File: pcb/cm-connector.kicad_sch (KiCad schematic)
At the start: 16 parts, among them J1 SODIMM-200, J2 Debug Connector/DNP

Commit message: remove components from the BOM which are DNP
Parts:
- J1, TP1, TP10, TP11, TP12, TP13, TP2, TP3, TP4, TP5, TP6: now left out of the parts list

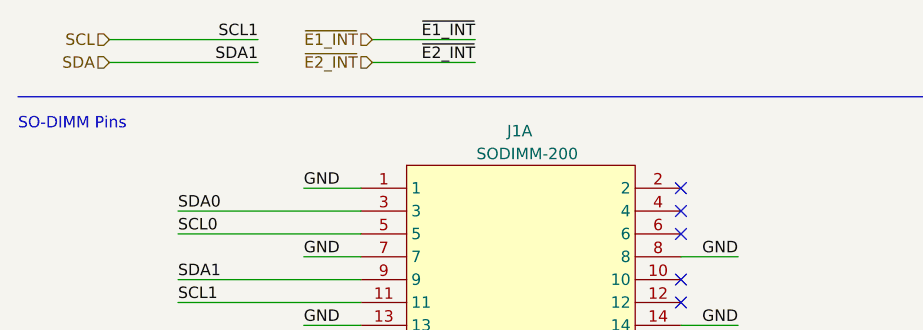
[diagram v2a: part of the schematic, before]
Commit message: Added jumper to swap I2C-0 with I2C-1 for the GPIO-Expanders
The GPIO expanders are using 0x20 and 0x21 as addresses and to avoid clashes with existing carrierboards I made the I2Cchannel switchable. Default is I2C-0 now
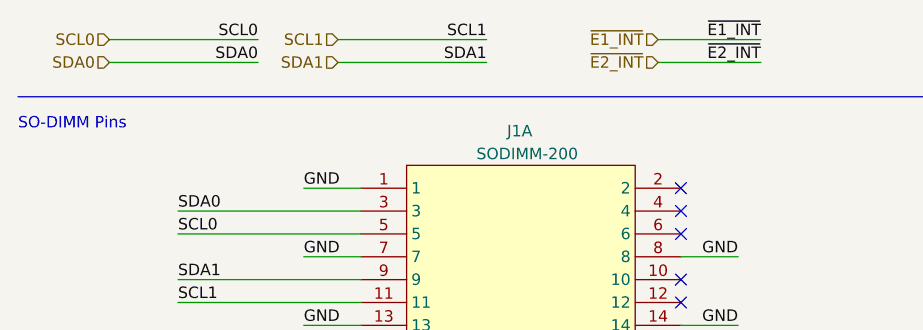
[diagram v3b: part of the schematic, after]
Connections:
- net SCL renamed SCL1
- net SDA renamed SDA1
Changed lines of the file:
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@@
     (stroke (width 0) (type default) (color 0 0 0 0))
   )
-  (wire (pts (xy 52.07 22.86) (xy 63.5 22.86))
+  (wire (pts (xy 83.82 22.86) (xy 95.25 22.86))
     (stroke (width 0) (type default) (color 0 0 0 0))
   )
@@
     (stroke (width 0) (type default) (color 0 0 0 0))
   )
+  (wire (pts (xy 48.26 20.32) (xy 64.77 20.32))
+    (stroke (width 0) (type default) (color 0 0 0 0))
+  )
   (wire (pts (xy 128.27 106.68) (xy 135.89 106.68))
     (stroke (width 0) (type default) (color 0 0 0 0))
@@
     (stroke (width 0) (type default) (color 0 0 0 0))
   )
-  (wire (pts (xy 52.07 20.32) (xy 63.5 20.32))
+  (wire (pts (xy 83.82 20.32) (xy 95.25 20.32))
     (stroke (width 0) (type default) (color 0 0 0 0))
   )
@@
     (stroke (width 0) (type default) (color 0 0 0 0))
   )
+  (wire (pts (xy 48.26 22.86) (xy 64.77 22.86))
+    (stroke (width 0) (type default) (color 0 0 0 0))
+  )
   (wire (pts (xy 66.04 160.02) (xy 86.36 160.02))
     (stroke (width 0) (type default) (color 0 0 0 0))
@@
     (effects (font (size 1.27 1.27)) (justify right bottom))
   )
-  (label "~{E2_INT}" (at 63.5 22.86 180)
+  (label "~{E2_INT}" (at 95.25 22.86 180)
     (effects (font (size 1.27 1.27)) (justify right bottom))
   )
@@
     (effects (font (size 1.27 1.27)) (justify right bottom))
   )
-  (label "~{E1_INT}" (at 63.5 20.32 180)
+  (label "~{E1_INT}" (at 95.25 20.32 180)
     (effects (font (size 1.27 1.27)) (justify right bottom))
   )
@@
     (effects (font (size 1.27 1.27)) (justify right bottom))
   )
+  (label "SCL1" (at 64.77 20.32 180)
+    (effects (font (size 1.27 1.27)) (justify right bottom))
+  )
   (label "V0SPI_MOSI" (at 30.48 77.47 0)
     (effects (font (size 1.27 1.27)) (justify left bottom))
@@
     (effects (font (size 1.27 1.27)) (justify left bottom))
   )
-  (label "SCL1" (at 39.37 20.32 180)
+  (label "SCL0" (at 39.37 20.32 180)
     (effects (font (size 1.27 1.27)) (justify right bottom))
   )
@@
     (effects (font (size 1.27 1.27)) (justify right bottom))
   )
+  (label "SDA1" (at 64.77 22.86 180)
+    (effects (font (size 1.27 1.27)) (justify right bottom))
+  )
   (label "GND" (at 129.54 71.12 0)
     (effects (font (size 1.27 1.27)) (justify left bottom))
   )
-  (label "SDA1" (at 39.37 22.86 180)
+  (label "SDA0" (at 39.37 22.86 180)
     (effects (font (size 1.27 1.27)) (justify right bottom))
   )
@@
     )
   )
-  (hierarchical_label "~{E2_INT}" (shape input) (at 52.07 22.86 180)
-    (effects (font (size 1.27 1.27)) (justify right))
-  )
-  (hierarchical_label "~{E1_INT}" (shape input) (at 52.07 20.32 180)
-    (effects (font (size 1.27 1.27)) (justify right))
-  )
-  (hierarchical_label "SDA" (shape input) (at 22.86 22.86 180)
-    (effects (font (size 1.27 1.27)) (justify right))
-  )
-  (hierarchical_label "SCL" (shape input) (at 22.86 20.32 180)
-    (effects (font (size 1.27 1.27)) (justify right))
-  )
+  (hierarchical_label "~{E2_INT}" (shape input) (at 83.82 22.86 180)
+    (effects (font (size 1.27 1.27)) (justify right))
+  )
+  (hierarchical_label "~{E1_INT}" (shape input) (at 83.82 20.32 180)
+    (effects (font (size 1.27 1.27)) (justify right))
+  )
+  (hierarchical_label "SDA1" (shape input) (at 48.26 22.86 180)
+    (effects (font (size 1.27 1.27)) (justify right))
+  )
+  (hierarchical_label "SDA0" (shape input) (at 22.86 22.86 180)
+    (effects (font (size 1.27 1.27)) (justify right))
+  )
+  (hierarchical_label "SCL0" (shape input) (at 22.86 20.32 180)
+    (effects (font (size 1.27 1.27)) (justify right))
+  )
+  (hierarchical_label "SCL1" (shape input) (at 48.26 20.32 180)
+    (effects (font (size 1.27 1.27)) (justify right))
+  )

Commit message: Refactored PCB Layer to have one dedicated GND Layer + rerouted traces + removed debug connector and added IO0 to the SO-DIMM connector + added decoupling caps and delay circuit for ESP32 module
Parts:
- removed J2: Debug Connector/DNP, Connector_PinSocket_2.54mm:PinSocket_1x06_P2.54mm_Vertical, symbol Connector:Conn_01x06_Male
- removed TP5: TP_3V3, TestPoint:TestPoint_Pad_D1.0mm, symbol Connector:TestPoint_Small
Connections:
- net IO0: now also J1.24
- no-connect marks 80 -> 79
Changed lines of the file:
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@@
   (junction (at 81.28 115.57) (diameter 0) (color 0 0 0 0)
   )
-  (junction (at 53.34 119.38) (diameter 0) (color 0 0 0 0)
-  )
   (junction (at 81.28 113.03) (diameter 0) (color 0 0 0 0)
   )
@@
   )
   (junction (at 109.22 113.03) (diameter 0) (color 0 0 0 0)
-  )
-  (junction (at 53.34 121.92) (diameter 0) (color 0 0 0 0)
   )
   (junction (at 109.22 110.49) (diameter 0) (color 0 0 0 0)
@@
   (no_connect (at 135.89 218.44))
   (no_connect (at 171.45 147.32))
-  (no_connect (at 86.36 64.77))
   (no_connect (at 135.89 149.86))
   (wire (pts (xy 66.04 199.39) (xy 86.36 199.39))
@@
     (stroke (width 0) (type default) (color 0 0 0 0))
   )
-  (wire (pts (xy 21.59 119.38) (xy 53.34 119.38))
+  (wire (pts (xy 27.94 109.22) (xy 53.34 109.22))
     (stroke (width 0) (type default) (color 0 0 0 0))
   )
@@
     (stroke (width 0) (type default) (color 0 0 0 0))
   )
-  (wire (pts (xy 21.59 121.92) (xy 53.34 121.92))
-    (stroke (width 0) (type default) (color 0 0 0 0))
-  )
   (wire (pts (xy 116.84 73.66) (xy 135.89 73.66))
     (stroke (width 0) (type default) (color 0 0 0 0))
@@
     (stroke (width 0) (type default) (color 0 0 0 0))
   )
+  (wire (pts (xy 27.94 116.84) (xy 53.34 116.84))
+    (stroke (width 0) (type default) (color 0 0 0 0))
+  )
   (wire (pts (xy 41.91 64.77) (xy 50.8 64.77))
     (stroke (width 0) (type default) (color 0 0 0 0))
@@
     (stroke (width 0) (type default) (color 0 0 0 0))
   )
-  (wire (pts (xy 21.59 116.84) (xy 53.34 116.84))
-    (stroke (width 0) (type default) (color 0 0 0 0))
-  )
   (wire (pts (xy 129.54 109.22) (xy 135.89 109.22))
     (stroke (width 0) (type default) (color 0 0 0 0))
@@
     (stroke (width 0) (type default) (color 0 0 0 0))
   )
+  (wire (pts (xy 86.36 64.77) (xy 92.71 64.77))
+    (stroke (width 0) (type default) (color 0 0 0 0))
+  )
   (wire (pts (xy 83.82 20.32) (xy 95.25 20.32))
     (stroke (width 0) (type default) (color 0 0 0 0))
@@
     (stroke (width 0) (type default) (color 0 0 0 0))
   )
-  (wire (pts (xy 21.59 109.22) (xy 53.34 109.22))
-    (stroke (width 0) (type default) (color 0 0 0 0))
-  )
   (wire (pts (xy 171.45 91.44) (xy 179.07 91.44))
     (stroke (width 0) (type default) (color 0 0 0 0))
@@
     (stroke (width 0) (type default) (color 0 0 0 0))
   )
-  (wire (pts (xy 66.04 104.14) (xy 66.04 121.92))
-    (stroke (width 0) (type default) (color 0 0 0 0))
-  )
   (wire (pts (xy 129.54 154.94) (xy 135.89 154.94))
     (stroke (width 0) (type default) (color 0 0 0 0))
   )
-  (wire (pts (xy 53.34 121.92) (xy 66.04 121.92))
-    (stroke (width 0) (type default) (color 0 0 0 0))
-  )
   (wire (pts (xy 177.8 132.08) (xy 171.45 132.08))
     (stroke (width 0) (type default) (color 0 0 0 0))
@@
     (stroke (width 0) (type default) (color 0 0 0 0))
   )
+  (wire (pts (xy 27.94 114.3) (xy 53.34 114.3))
+    (stroke (width 0) (type default) (color 0 0 0 0))
+  )
   (wire (pts (xy 53.34 119.38) (xy 54.61 119.38))
     (stroke (width 0) (type default) (color 0 0 0 0))
@@
     (stroke (width 0) (type default) (color 0 0 0 0))
   )
-  (wire (pts (xy 21.59 114.3) (xy 53.34 114.3))
-    (stroke (width 0) (type default) (color 0 0 0 0))
-  )
   (wire (pts (xy 189.23 241.3) (xy 189.23 243.84))
     (stroke (width 0) (type default) (color 0 0 0 0))
   )
+  (wire (pts (xy 27.94 111.76) (xy 53.34 111.76))
+    (stroke (width 0) (type default) (color 0 0 0 0))
+  )
   (wire (pts (xy 66.04 179.07) (xy 86.36 179.07))
     (stroke (width 0) (type default) (color 0 0 0 0))
@@
     (stroke (width 0) (type default) (color 0 0 0 0))
   )
-  (wire (pts (xy 21.59 111.76) (xy 53.34 111.76))
-    (stroke (width 0) (type default) (color 0 0 0 0))
-  )
   (wire (pts (xy 66.04 204.47) (xy 86.36 204.47))
     (stroke (width 0) (type default) (color 0 0 0 0))
@@
     (effects (font (size 1.27 1.27)) (justify left bottom))
   )
-  (label "TXD0" (at 40.64 116.84 180)
-    (effects (font (size 1.27 1.27)) (justify right bottom))
+  (label "TXD0" (at 27.94 116.84 0)
+    (effects (font (size 1.27 1.27)) (justify left bottom))
   )
   (label "GND" (at 177.8 223.52 180)
@@
     (effects (font (size 1.27 1.27)) (justify left bottom))
   )
-  (label "RXD0" (at 40.64 114.3 180)
-    (effects (font (size 1.27 1.27)) (justify right bottom))
+  (label "RXD0" (at 27.94 114.3 0)
+    (effects (font (size 1.27 1.27)) (justify left bottom))
   )
   (label "SCL1" (at 30.48 49.53 0)
@@
     (effects (font (size 1.27 1.27)) (justify right bottom))
   )
+  (label "IO0" (at 92.71 64.77 180)
+    (effects (font (size 1.27 1.27)) (justify right bottom))
+  )
   (label "SCL1" (at 64.77 20.32 180)
     (effects (font (size 1.27 1.27)) (justify right bottom))
@@
     (effects (font (size 1.27 1.27)) (justify right bottom))
   )
-  (label "IO0" (at 40.64 111.76 180)
-    (effects (font (size 1.27 1.27)) (justify right bottom))
+  (label "IO0" (at 27.94 111.76 0)
+    (effects (font (size 1.27 1.27)) (justify left bottom))
   )
   (label "GND" (at 44.45 67.31 0)
@@
     (effects (font (size 1.27 1.27)) (justify left bottom))
   )
-  (label "ESP_EN{slash}CM_RUN" (at 40.64 109.22 180)
-    (effects (font (size 1.27 1.27)) (justify right bottom))
+  (label "ESP_EN{slash}CM_RUN" (at 27.94 109.22 0)
+    (effects (font (size 1.27 1.27)) (justify left bottom))
   )
   (label "SCL1" (at 86.36 186.69 180)
@@
   (hierarchical_label "SCL1" (shape input) (at 48.26 20.32 180)
     (effects (font (size 1.27 1.27)) (justify right))
-  )
-  (symbol (lib_id "Connector:Conn_01x06_Male") (at 16.51 114.3 0) (unit 1)
-    (in_bom no) (on_board yes)
-    (property "Reference" "J2" (id 0) (at 26.67 101.6 0))
-    (property "Value" "Debug Connector/DNP" (id 1) (at 26.67 104.14 0))
-    (property "Footprint" "Connector_PinSocket_2.54mm:PinSocket_1x06_P2.54mm_Vertical" (id 2) (at 16.51 114.3 0)
-      (effects (font (size 1.27 1.27)) hide)
-    )
-    (property "Datasheet" "~" (id 3) (at 16.51 114.3 0)
-      (effects (font (size 1.27 1.27)) hide)
-    )
-    (pin "1")
-    (pin "2")
-    (pin "3")
-    (pin "4")
-    (pin "5")
-    (pin "6")
   )
   (symbol (lib_id "Connector:TestPoint_Small") (at 81.28 118.11 0) (unit 1)
@@
     )
     (property "Datasheet" "~" (id 3) (at 86.36 115.57 0)
-      (effects (font (size 1.27 1.27)) hide)
-    )
-    (pin "1")
-  )
-  (symbol (lib_id "Connector:TestPoint_Small") (at 53.34 121.92 0) (unit 1)
-    (in_bom no) (on_board yes)
-    (property "Reference" "TP5" (id 0) (at 49.53 120.65 0)
-      (effects (font (size 1.27 1.27)) (justify left))
-    )
-    (property "Value" "TP_3V3" (id 1) (at 55.88 123.19 0)
-      (effects (font (size 1.27 1.27)) (justify left))
-    )
-    (property "Footprint" "TestPoint:TestPoint_Pad_D1.0mm" (id 2) (at 58.42 121.92 0)
-      (effects (font (size 1.27 1.27)) hide)
-    )
-    (property "Datasheet" "~" (id 3) (at 58.42 121.92 0)
       (effects (font (size 1.27 1.27)) hide)
     )
@@
       (effects (font (size 1.27 1.27)) hide)
     )
-    (pin "1")
-  )
-  (symbol (lib_id "power:+3V3") (at 66.04 104.14 0) (unit 1)
-    (in_bom yes) (on_board yes) (fields_autoplaced)
-    (property "Reference" "#PWR0119" (id 0) (at 66.04 107.95 0)
-      (effects (font (size 1.27 1.27)) hide)
-    )
-    (property "Value" "+3V3" (id 1) (at 66.04 100.5355 0))
-    (property "Footprint" "" (id 2) (at 66.04 104.14 0)
-      (effects (font (size 1.27 1.27)) hide)
-    )
-    (property "Datasheet" "" (id 3) (at 66.04 104.14 0)
-      (effects (font (size 1.27 1.27)) hide)
-    )

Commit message: Convert to KiCad 7
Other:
- note added: "Test Point"
- note removed: "Debug Connector"
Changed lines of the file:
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@@
+    (stroke (width 0) (type default) (color 0 0 0 0))
+  )
+  (wire (pts (xy 53.34 119.38) (xy 53.34 121.92))
     (stroke (width 0) (type default) (color 0 0 0 0))
   )
@@
     (stroke (width 0) (type default) (color 0 0 0 0))
   )
-  (wire (pts (xy 54.61 119.38) (xy 54.61 127))
-    (stroke (width 0) (type default) (color 0 0 0 0))
-  )
   (wire (pts (xy 116.84 66.04) (xy 135.89 66.04))
     (stroke (width 0) (type default) (color 0 0 0 0))
@@
     (stroke (width 0) (type default) (color 0 0 0 0))
   )
-  (wire (pts (xy 53.34 119.38) (xy 54.61 119.38))
-    (stroke (width 0) (type default) (color 0 0 0 0))
-  )
   (wire (pts (xy 171.45 45.72) (xy 179.07 45.72))
     (stroke (width 0) (type default) (color 0 0 0 0))
@@
     (effects (font (size 1.27 1.27)) (justify left bottom))
   )
-  (text "Debug Connector" (at 13.97 95.25 0)
+  (text "Test Point" (at 13.97 95.25 0)
     (effects (font (size 1.27 1.27)) (justify left bottom))
   )
@@
       (effects (font (size 1.27 1.27)) (justify left))
     )
-    (property "Value" "TP_IO0" (id 1) (at 55.88 111.76 0)
+    (property "Value" "TP_IO0" (id 1) (at 54.61 111.76 0)
       (effects (font (size 1.27 1.27)) (justify left))
     )
@@
     (pin "1")
   )
-  (symbol (lib_id "power:GND") (at 54.61 127 0) (unit 1)
+  (symbol (lib_id "power:GND") (at 53.34 121.92 0) (unit 1)
     (in_bom yes) (on_board yes) (fields_autoplaced)
-    (property "Reference" "#PWR0118" (id 0) (at 54.61 133.35 0)
-      (effects (font (size 1.27 1.27)) hide)
-    )
-    (property "Value" "GND" (id 1) (at 54.61 131.5625 0))
-    (property "Footprint" "" (id 2) (at 54.61 127 0)
-      (effects (font (size 1.27 1.27)) hide)
-    )
-    (property "Datasheet" "" (id 3) (at 54.61 127 0)
+    (property "Reference" "#PWR0118" (id 0) (at 53.34 128.27 0)
+      (effects (font (size 1.27 1.27)) hide)
+    )
+    (property "Value" "GND" (id 1) (at 53.34 126.4825 0))
+    (property "Footprint" "" (id 2) (at 53.34 121.92 0)
+      (effects (font (size 1.27 1.27)) hide)
+    )
+    (property "Datasheet" "" (id 3) (at 53.34 121.92 0)
       (effects (font (size 1.27 1.27)) hide)
     )
@@
       (effects (font (size 1.27 1.27)) (justify left))
     )
-    (property "Value" "TP_EN" (id 1) (at 55.88 109.22 0)
+    (property "Value" "TP_EN" (id 1) (at 54.61 109.22 0)
       (effects (font (size 1.27 1.27)) (justify left))
     )
@@
       (effects (font (size 1.27 1.27)) (justify left))
     )
-    (property "Value" "TP_RX" (id 1) (at 55.88 114.3 0)
+    (property "Value" "TP_RX" (id 1) (at 54.61 114.3 0)
       (effects (font (size 1.27 1.27)) (justify left))
     )
@@
       (effects (font (size 1.27 1.27)) (justify left))
     )
-    (property "Value" "TP_GND" (id 1) (at 55.88 119.38 0)
+    (property "Value" "TP_GND" (id 1) (at 54.61 119.38 0)
       (effects (font (size 1.27 1.27)) (justify left))
     )
@@
       (effects (font (size 1.27 1.27)) (justify left))
     )
-    (property "Value" "TP_TX" (id 1) (at 55.88 116.84 0)
-      (effects (font (size 1.27 1.27)) (justify left))
-    )
+    (property "Value" "TP_TX" (id 1) (at 54.61 116.84 0)
+      (effects (font (size 1.27 1.27)) (justify left))
+    )
